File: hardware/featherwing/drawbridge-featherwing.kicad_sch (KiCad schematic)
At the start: 12 parts, among them J1 Feather 16, J2 Feather 12, J3 OUT / GND, Q1 2N3904

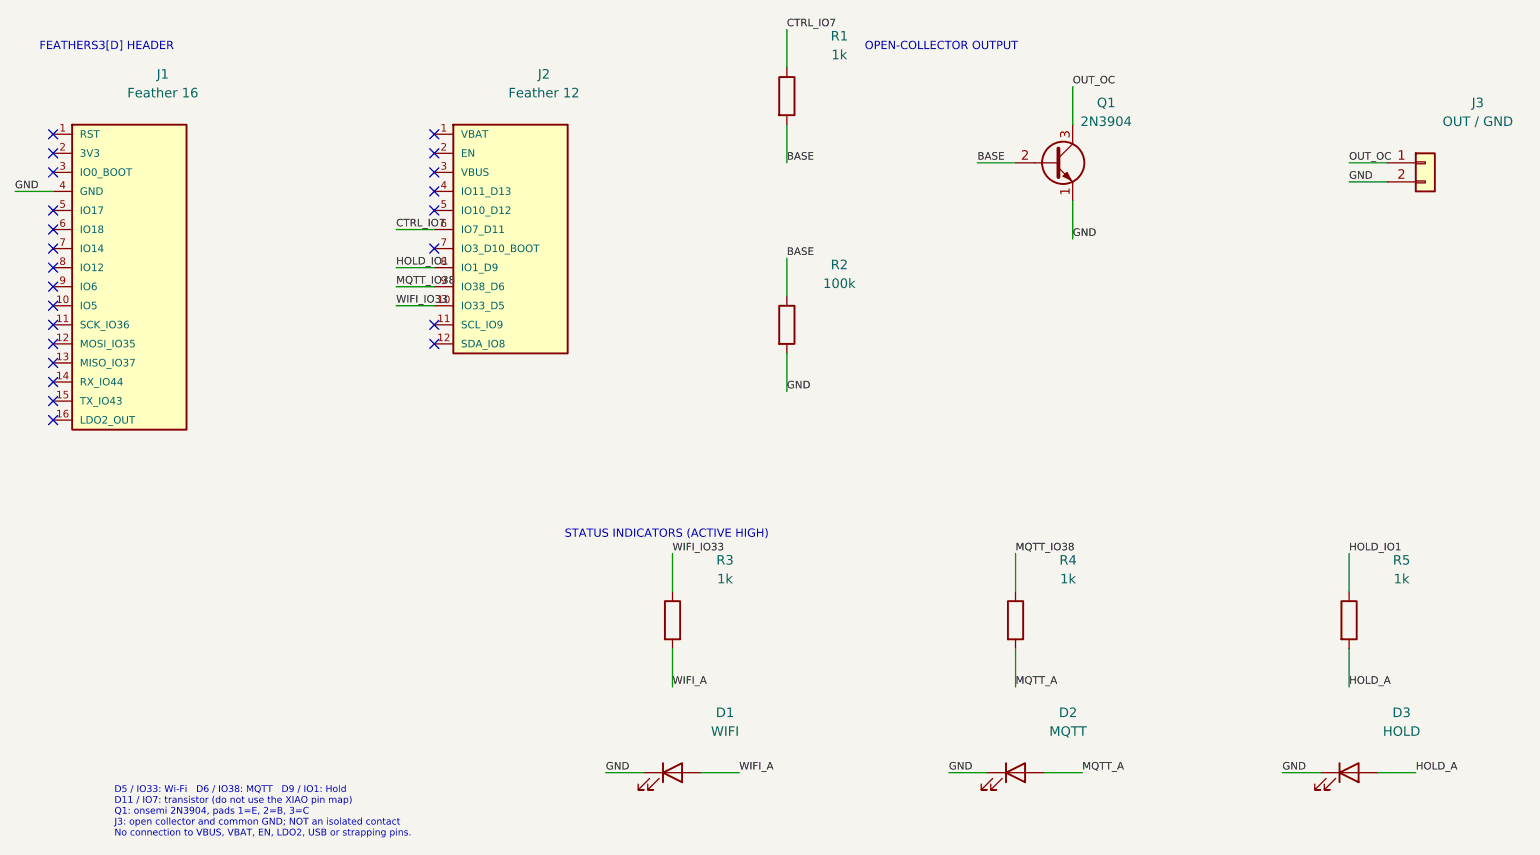
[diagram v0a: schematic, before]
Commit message: Finalize FeatherWing fabrication design
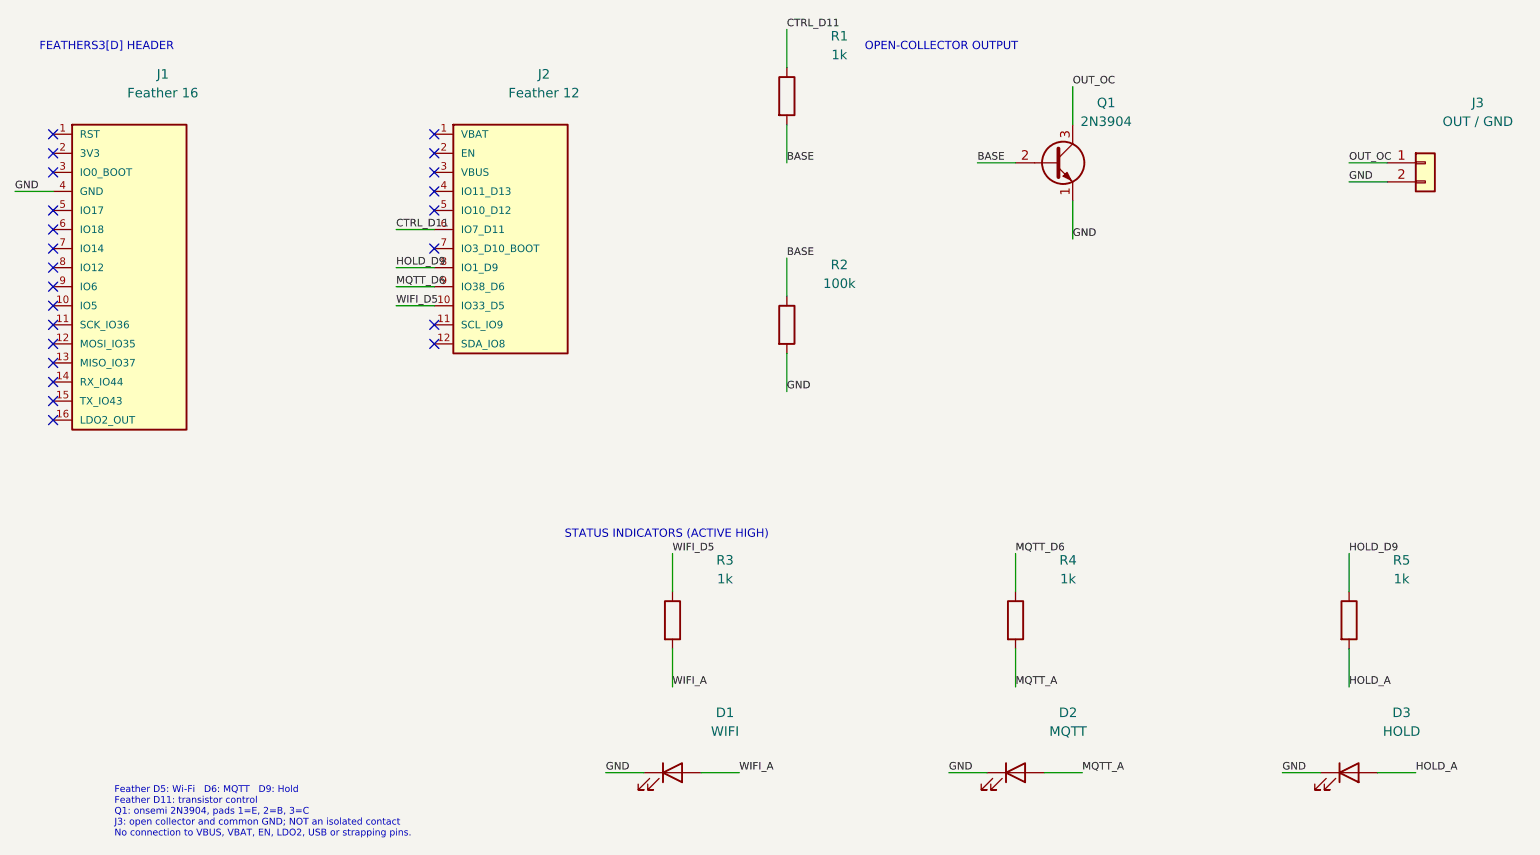
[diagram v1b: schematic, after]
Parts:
- J3: footprint Drawbridge:GateOutputHeader -> Drawbridge:GateOutputPads
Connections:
- net CTRL_IO7 renamed CTRL_D11
- net HOLD_IO1 renamed HOLD_D9
- net MQTT_IO38 renamed MQTT_D6
- net WIFI_IO33 renamed WIFI_D5
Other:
- note added: "Feather D5: Wi-Fi D6: MQTT D9: Hold Feather D11: transistor control Q1: onsemi 2N3904, pads 1=E, 2=B, 3=C J3: open collector and common GND; NOT an isolated contact No connection to VBUS, VBAT, EN, LDO2, USB or strapping pins."
- note removed: "D5 / IO33: Wi-Fi D6 / IO38: MQTT D9 / IO1: Hold D11 / IO7: transistor (do not use the XIAO pin map) Q1: onsemi 2N3904, pads 1=E, 2=B, 3=C J3: open collector and common GND; NOT an isolated contact No connection to VBUS, VBAT, EN, LDO2, USB or strapping pins."
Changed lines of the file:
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@@
 (kicad_sch (version 20250114) (generator "eeschema") (paper "A4")
-(title_block (title "Drawbridge FeatherWing - FeatherS3[D]") (rev "A DRAFT") (comment 1 "USB-powered host; no Feather module in assembly BOM") (comment 2 "Prototype open-collector output; gate interface not released"))
+(title_block (title "Drawbridge FeatherWing - FeatherS3[D]") (rev "d4f.9") (comment 1 "USB-powered host; no Feather module in assembly BOM") (comment 2 "Prototype open-collector output; gate interface not released"))
 (symbol (lib_id "Drawbridge:Feather16") (at 44.45 54.61 0) (unit 1) (in_bom yes) (on_board yes) (dnp no)
 (property "Reference" "J1" (at 51.45 46.61 0) (effects (font (size 1.27 1.27)) ))
@@
 (no_connect (at 87.63 64.77))
 (wire (pts (xy 87.63 67.31) (xy 82.55 67.31)) (stroke (width 0) (type default)))
-(label "CTRL_IO7" (at 82.55 67.31 0) (effects (font (size 1 1)) (justify left bottom)))
+(label "CTRL_D11" (at 82.55 67.31 0) (effects (font (size 1 1)) (justify left bottom)))
 (no_connect (at 87.63 69.85))
 (wire (pts (xy 87.63 72.39) (xy 82.55 72.39)) (stroke (width 0) (type default)))
-(label "HOLD_IO1" (at 82.55 72.39 0) (effects (font (size 1 1)) (justify left bottom)))
+(label "HOLD_D9" (at 82.55 72.39 0) (effects (font (size 1 1)) (justify left bottom)))
 (wire (pts (xy 87.63 74.93) (xy 82.55 74.93)) (stroke (width 0) (type default)))
-(label "MQTT_IO38" (at 82.55 74.93 0) (effects (font (size 1 1)) (justify left bottom)))
+(label "MQTT_D6" (at 82.55 74.93 0) (effects (font (size 1 1)) (justify left bottom)))
 (wire (pts (xy 87.63 77.47) (xy 82.55 77.47)) (stroke (width 0) (type default)))
-(label "WIFI_IO33" (at 82.55 77.47 0) (effects (font (size 1 1)) (justify left bottom)))
+(label "WIFI_D5" (at 82.55 77.47 0) (effects (font (size 1 1)) (justify left bottom)))
 (no_connect (at 87.63 80.00999999999999))
 (no_connect (at 87.63 82.55))
@@
 (instances (project "drawbridge-featherwing" (path "/e045a70d-6a43-543a-bb83-4cd8dfb407e3" (reference "R1") (unit 1)))))
 (wire (pts (xy 134.62 45.72) (xy 134.62 40.64)) (stroke (width 0) (type default)))
-(label "CTRL_IO7" (at 134.62 40.64 0) (effects (font (size 1 1)) (justify left bottom)))
+(label "CTRL_D11" (at 134.62 40.64 0) (effects (font (size 1 1)) (justify left bottom)))
 (wire (pts (xy 134.62 53.34) (xy 134.62 58.42)) (stroke (width 0) (type default)))
 (label "BASE" (at 134.62 58.42 0) (effects (font (size 1 1)) (justify left bottom)))
@@
 (property "Reference" "J3" (at 226.71 50.42 0) (effects (font (size 1.27 1.27)) ))
 (property "Value" "OUT / GND" (at 226.71 52.92 0) (effects (font (size 1.27 1.27)) ))
-(property "Footprint" "Drawbridge:GateOutputHeader" (at 226.71 58.42 0) (effects (font (size 1.27 1.27)) hide))
+(property "Footprint" "Drawbridge:GateOutputPads" (at 226.71 58.42 0) (effects (font (size 1.27 1.27)) hide))
 (instances (project "drawbridge-featherwing" (path "/e045a70d-6a43-543a-bb83-4cd8dfb407e3" (reference "J3") (unit 1)))))
 (wire (pts (xy 214.63 58.42) (xy 209.55 58.42)) (stroke (width 0) (type default)))
@@
 (instances (project "drawbridge-featherwing" (path "/e045a70d-6a43-543a-bb83-4cd8dfb407e3" (reference "R3") (unit 1)))))
 (wire (pts (xy 119.38 115.57) (xy 119.38 110.49)) (stroke (width 0) (type default)))
-(label "WIFI_IO33" (at 119.38 110.49 0) (effects (font (size 1 1)) (justify left bottom)))
+(label "WIFI_D5" (at 119.38 110.49 0) (effects (font (size 1 1)) (justify left bottom)))
 (wire (pts (xy 119.38 123.19) (xy 119.38 128.27)) (stroke (width 0) (type default)))
 (label "WIFI_A" (at 119.38 128.27 0) (effects (font (size 1 1)) (justify left bottom)))
@@
 (instances (project "drawbridge-featherwing" (path "/e045a70d-6a43-543a-bb83-4cd8dfb407e3" (reference "R4") (unit 1)))))
 (wire (pts (xy 165.1 115.57) (xy 165.1 110.49)) (stroke (width 0) (type default)))
-(label "MQTT_IO38" (at 165.1 110.49 0) (effects (font (size 1 1)) (justify left bottom)))
+(label "MQTT_D6" (at 165.1 110.49 0) (effects (font (size 1 1)) (justify left bottom)))
 (wire (pts (xy 165.1 123.19) (xy 165.1 128.27)) (stroke (width 0) (type default)))
 (label "MQTT_A" (at 165.1 128.27 0) (effects (font (size 1 1)) (justify left bottom)))
@@
 (instances (project "drawbridge-featherwing" (path "/e045a70d-6a43-543a-bb83-4cd8dfb407e3" (reference "R5") (unit 1)))))
 (wire (pts (xy 209.55 115.57) (xy 209.55 110.49)) (stroke (width 0) (type default)))
-(label "HOLD_IO1" (at 209.55 110.49 0) (effects (font (size 1 1)) (justify left bottom)))
+(label "HOLD_D9" (at 209.55 110.49 0) (effects (font (size 1 1)) (justify left bottom)))
 (wire (pts (xy 209.55 123.19) (xy 209.55 128.27)) (stroke (width 0) (type default)))
 (label "HOLD_A" (at 209.55 128.27 0) (effects (font (size 1 1)) (justify left bottom)))
@@
 (text "OPEN-COLLECTOR OUTPUT" (at 145 43 0) (effects (font (size 1.1 1.1)) (justify left)))
 (text "STATUS INDICATORS (ACTIVE HIGH)" (at 105 108 0) (effects (font (size 1.1 1.1)) (justify left)))
-(text "D5 / IO33: Wi-Fi   D6 / IO38: MQTT   D9 / IO1: Hold\nD11 / IO7: transistor (do not use the XIAO pin map)\nQ1: onsemi 2N3904, pads 1=E, 2=B, 3=C\nJ3: open collector and common GND; NOT an isolated contact\nNo connection to VBUS, VBAT, EN, LDO2, USB or strapping pins." (at 45 145 0) (effects (font (size 0.9 0.9)) (justify left)))
+(text "Feather D5: Wi-Fi   D6: MQTT   D9: Hold\nFeather D11: transistor control\nQ1: onsemi 2N3904, pads 1=E, 2=B, 3=C\nJ3: open collector and common GND; NOT an isolated contact\nNo connection to VBUS, VBAT, EN, LDO2, USB or strapping pins." (at 45 145 0) (effects (font (size 0.9 0.9)) (justify left)))
 (embedded_fonts no))

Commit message: Use a screw terminal and 45-degree routing on the FeatherWing
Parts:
- J3: footprint Drawbridge:GateOutputPads -> Drawbridge:ExitTerminal
- R5: footprint Drawbridge:GateHoldResistor -> Resistor_THT:R_Axial_DIN0207_L6.3mm_D2.5mm_P7.62mm_Horizontal
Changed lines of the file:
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@@
 (kicad_sch (version 20250114) (generator "eeschema") (paper "A4")
-(title_block (title "Drawbridge FeatherWing - FeatherS3[D]") (rev "d4f.9") (comment 1 "USB-powered host; no Feather module in assembly BOM") (comment 2 "Prototype open-collector output; gate interface not released"))
+(title_block (title "Drawbridge FeatherWing - FeatherS3[D]") (rev "748.5") (comment 1 "USB-powered host; no Feather module in assembly BOM") (comment 2 "Prototype open-collector output; gate interface not released"))
 (symbol (lib_id "Drawbridge:Feather16") (at 44.45 54.61 0) (unit 1) (in_bom yes) (on_board yes) (dnp no)
 (property "Reference" "J1" (at 51.45 46.61 0) (effects (font (size 1.27 1.27)) ))
@@
 (property "Reference" "J3" (at 226.71 50.42 0) (effects (font (size 1.27 1.27)) ))
 (property "Value" "OUT / GND" (at 226.71 52.92 0) (effects (font (size 1.27 1.27)) ))
-(property "Footprint" "Drawbridge:GateOutputPads" (at 226.71 58.42 0) (effects (font (size 1.27 1.27)) hide))
+(property "Footprint" "Drawbridge:ExitTerminal" (at 226.71 58.42 0) (effects (font (size 1.27 1.27)) hide))
 (instances (project "drawbridge-featherwing" (path "/e045a70d-6a43-543a-bb83-4cd8dfb407e3" (reference "J3") (unit 1)))))
 (wire (pts (xy 214.63 58.42) (xy 209.55 58.42)) (stroke (width 0) (type default)))
@@
 (property "Reference" "R5" (at 216.55 111.38 0) (effects (font (size 1.27 1.27)) ))
 (property "Value" "1k" (at 216.55 113.88 0) (effects (font (size 1.27 1.27)) ))
-(property "Footprint" "Drawbridge:GateHoldResistor" (at 216.55 119.38 0) (effects (font (size 1.27 1.27)) hide))
+(property "Footprint" "Resistor_THT:R_Axial_DIN0207_L6.3mm_D2.5mm_P7.62mm_Horizontal" (at 216.55 119.38 0) (effects (font (size 1.27 1.27)) hide))
 (instances (project "drawbridge-featherwing" (path "/e045a70d-6a43-543a-bb83-4cd8dfb407e3" (reference "R5") (unit 1)))))
 (wire (pts (xy 209.55 115.57) (xy 209.55 110.49)) (stroke (width 0) (type default)))
